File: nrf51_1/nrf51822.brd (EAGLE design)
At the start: 40 x 27.8 mm, 22 parts, among them T1 MMUN2238

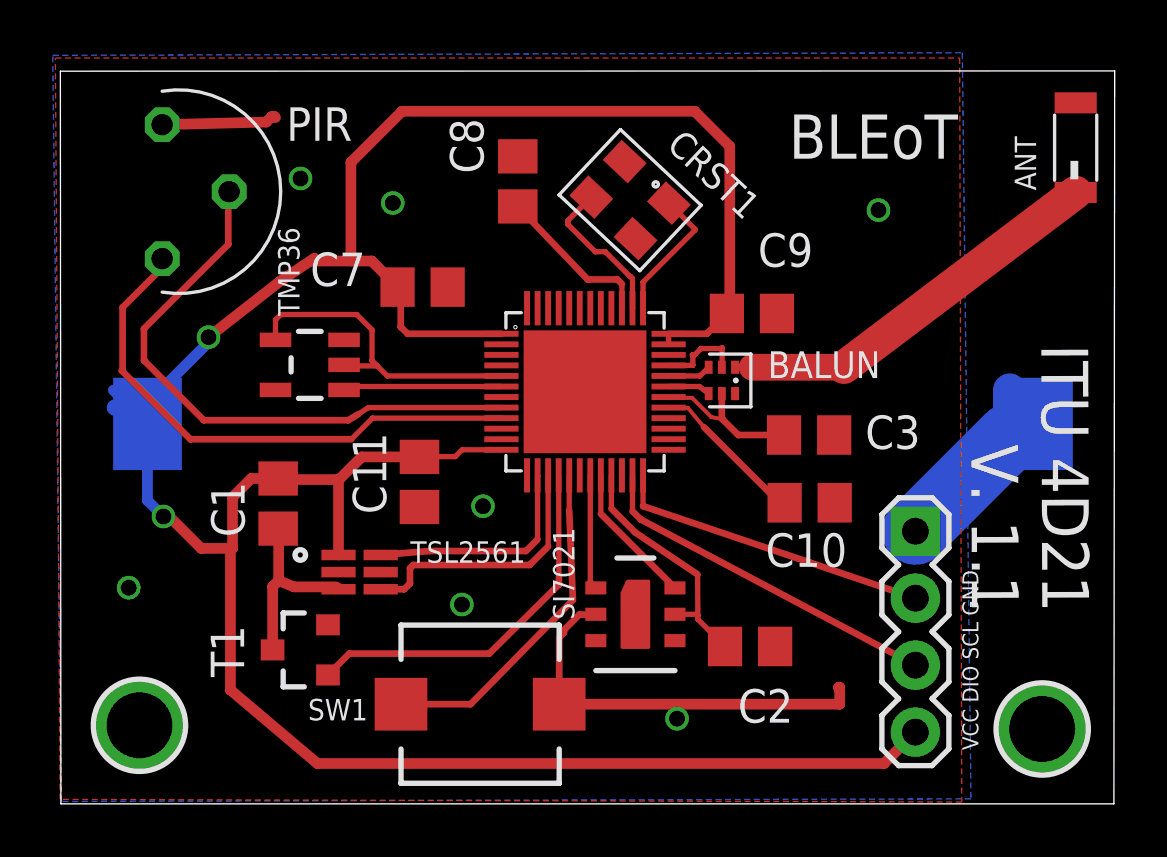
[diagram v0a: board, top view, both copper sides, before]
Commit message: Sensor board should be 100% done... Waiting for boards from slow china :0)
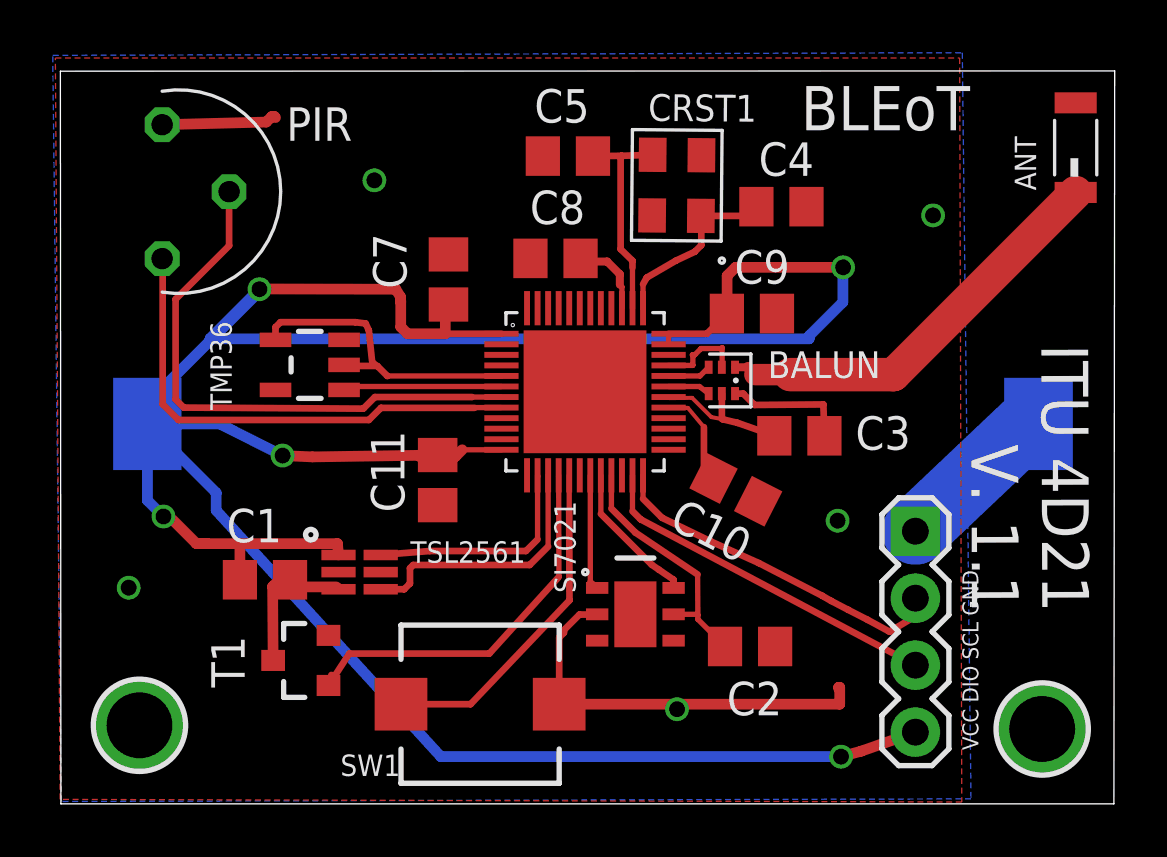
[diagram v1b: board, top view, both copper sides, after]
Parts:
- added C4, C5: 12pF, rcl:C0805
- moved C8 3.25 mm to (20.3, 22.5), turned to 0 degrees
- moved C1 2.93 mm to (9.25, 10.3), turned to 180 degrees
- moved C10 2.84 mm to (27.1, 13.7), turned to 333 degrees
- moved CRST1 1.86 mm to (24.9, 25.3), turned to 89.5 degrees
- moved C7 1.02 mm to (16.2, 21.7), turned to 90 degrees
- moved C11 0.69 mm to (15.8, 14.1)
- moved T1 0.40 mm to (10.7, 7.25)
- moved C3 0.37 mm to (29.5, 15.8)
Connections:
- net AIN4: now also PIR.2
- net AIN5: now also PIR.1; no longer PIR.2
- net AIN6: no longer PIR.1
- net GND: now also C4.1, C5.1
- net N$1: now also C5.2, CRST1.H2, U$4.38; no longer CRST1.H1, U$4.37
- net N$2: now also C4.2, CRST1.H1, U$4.37; no longer CRST1.H2, U$4.38
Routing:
- net AIN4: track 0.00 -> 21.4 mm
- net AIN6: track 20.7 -> 0.00 mm
- net VDD: track 108.3 -> 124.5 mm, vias 2 -> 5
- net GND: track 31.9 -> 39.2 mm, vias 7 -> 5
- net AIN5: track 22.4 -> 18.8 mm
- net N$1: track 5.21 -> 8.25 mm
- net N$5: track 6.12 -> 3.09 mm
- net N$13: track 5.93 -> 3.78 mm
- net N$2: track 5.84 -> 7.20 mm
- net N$14: track 12.1 -> 13.4 mm
- net N$3: track 15.1 -> 15.9 mm
- net N$4: track 5.93 -> 5.42 mm
- net GIOP2: track 14.4 -> 14.9 mm
